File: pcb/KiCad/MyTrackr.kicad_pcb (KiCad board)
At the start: 2 copper layers, 50 x 50 mm, 38 parts, among them CN1 GPS_ANTENNA, CON1 MICRO_SD, J1 10A45B_Module, J2 CONN_ICSP, J3 CONN_01X05, J4 CONN_BAT, P1 CONN_OLED, Q1 Q_PMOS_GSD, SW1 BTN_RESET, SW2 BTN_SEL, SW3 BTN_NEXT, SW4 BTN_PREV, SW5 BTN_BACK, U1 ATMEGA48_88_168_328P-32SMD, U2 GPS-NEO-6M, U3 24AA32

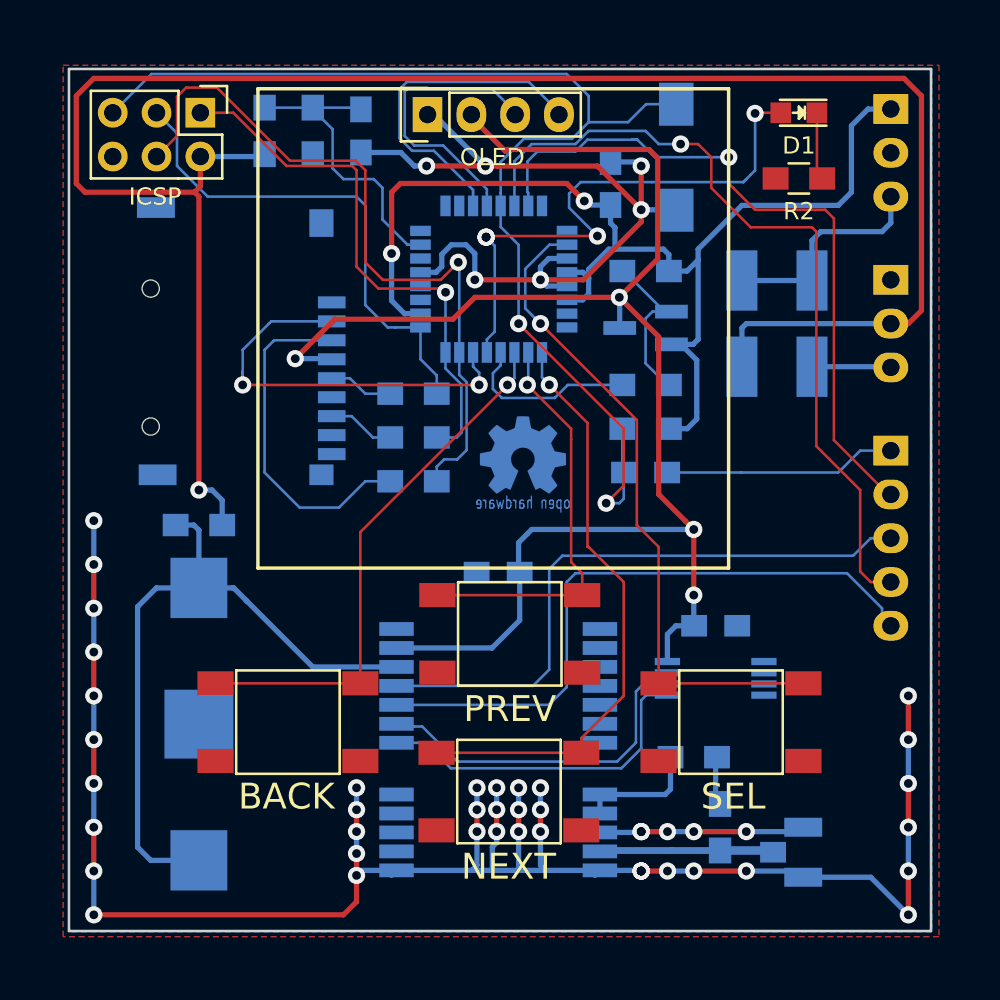
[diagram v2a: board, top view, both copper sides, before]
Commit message: Add screw holes, smooth corners and more
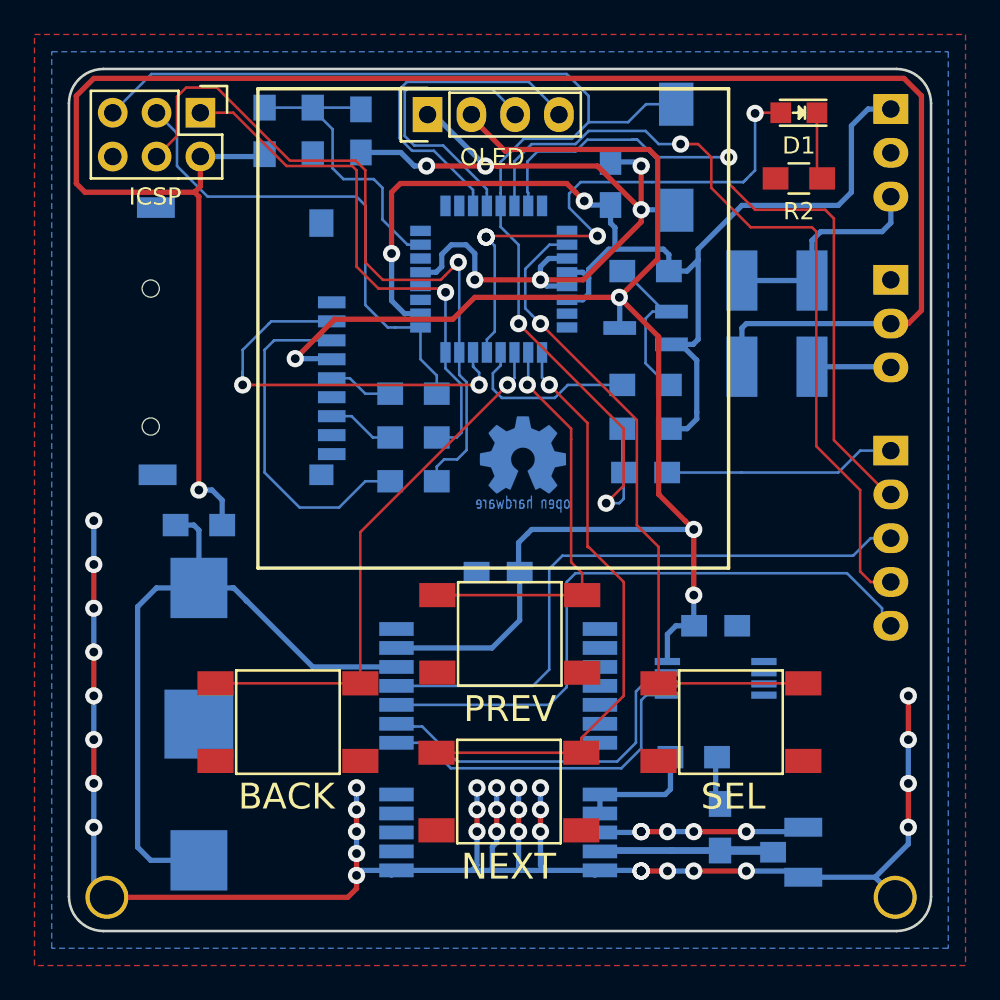
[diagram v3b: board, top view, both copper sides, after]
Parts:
- added P2: CONN_01X01, Sukko:Screw_Hole_Plated_2mm, F.Cu at (137.9, 98.0)
- added P3: CONN_01X01, Sukko:Screw_Hole_Plated_2mm, F.Cu at (92.2, 98.0)
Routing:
- net GND: track 174.0 -> 169.4 mm, vias 51 -> 47
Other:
- outline, holes or cut-outs redrawn
- board text added: "github.com/SukkoPera/MyTrackr"
- board text removed: "https://github.com/SukkoPera/MyTrackr"
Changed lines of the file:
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@@
 (kicad_pcb (version 4) (host pcbnew 4.0.7)
   (general
-    (links 103)
-    (no_connects 0)
+    (links 107)
+    (no_connects 28)
     (area 89.924999 49.924999 140.075001 100.075001)
     (thickness 1.6)
-    (drawings 39)
-    (tracks 586)
+    (drawings 43)
+    (tracks 582)
     (zones 0)
-    (modules 38)
+    (modules 40)
     (nets 37)
   )
@@
     (mod_text_size 1 1)
     (mod_text_width 0.15)
-    (pad_size 2 0.8)
-    (pad_drill 0)
+    (pad_size 2.5 2.5)
+    (pad_drill 2)
     (pad_to_mask_clearance 0)
     (aux_axis_origin 0 0)
@@
     (tags "resistor 0805")
     (attr smd)
-    (fp_text reference JP1 (at 3.81 0) (layer B.SilkS)
+    (fp_text reference JP1 (at -3.81 0) (layer B.SilkS)
       (effects (font (size 1 1) (thickness 0.15)) (justify mirror))
     )
@@
     (at 127.508 85.344 270)
     (descr TSSOP-8)
-    (fp_text reference U3 (at -2.286 -3.556 360) (layer B.SilkS)
+    (fp_text reference U3 (at 0 -4.826 360) (layer B.SilkS)
       (effects (font (size 1 1) (thickness 0.15)) (justify mirror))
     )
@@
     (pad 8 smd rect (at -0.97536 2.79908 270) (size 0.4191 1.47066) (layers B.Cu B.Mask)
       (net 33 VPP))
-    (model walter/smd_dil/tssop-8.wrl
-      (at (xyz 0 0 0))
-      (scale (xyz 1 1 1))
-      (rotate (xyz 0 0 0))
-    )
-  )
+    (model /home/sukko/Documents/kicad/lib/kicad_libs/modules/packages3d/walter/smd_dil/tssop-8.wrl
+      (at (xyz 0 0 0))
+      (scale (xyz 1 1 1))
+      (rotate (xyz 0 0 0))
+    )
+  )
+  (module Sukko:Screw_Hole_Plated_2mm (layer F.Cu)
+    (at 137.922 98.044)
+    (fp_text reference P2 (at 0 2.54) (layer F.SilkS) hide
+      (effects (font (size 1 1) (thickness 0.15)))
+    )
+    (fp_text value CONN_01X01 (at 0 5.08) (layer F.Fab) hide
+      (effects (font (size 1 1) (thickness 0.15)))
+    )
+    (pad 1 thru_hole circle (at 0 0) (size 2.5 2.5) (drill 2) (layers *.Cu *.Mask)
+      (net 2 GND) (zone_connect 2))
+  )
+  (module Sukko:Screw_Hole_Plated_2mm (layer F.Cu)
+    (at 92.202 98.044)
+    (fp_text reference P3 (at 0 2.54) (layer F.SilkS) hide
+      (effects (font (size 1 1) (thickness 0.15)))
+    )
+    (fp_text value CONN_01X01 (at 0 5.08) (layer F.Fab) hide
+      (effects (font (size 1 1) (thickness 0.15)))
+    )
+    (pad 1 thru_hole circle (at 0 0) (size 2.5 2.5) (drill 2) (layers *.Cu *.Mask)
+      (net 2 GND) (zone_connect 2))
+  )
+  (gr_arc (start 92 52) (end 90 52) (angle 90) (layer Edge.Cuts) (width 0.15))
+  (gr_arc (start 138 52) (end 138 50) (angle 90) (layer Edge.Cuts) (width 0.15))
+  (gr_arc (start 138 98) (end 140 98) (angle 90) (layer Edge.Cuts) (width 0.15))
+  (gr_arc (start 92 98) (end 92 100) (angle 90) (layer Edge.Cuts) (width 0.15))
   (gr_text OLED (at 114.554 55.118) (layer F.SilkS)
     (effects (font (size 1 1) (thickness 0.15)))
@@
     (effects (font (size 1 1) (thickness 0.15)))
   )
-  (gr_text Vi (at 135.474 57.404 360) (layer B.SilkS)
+  (gr_text Vi (at 135.474 57.404) (layer B.SilkS)
     (effects (font (size 0.7 0.7) (thickness 0.1)) (justify mirror))
   )
@@
     (effects (font (size 1 1) (thickness 0.15)) (justify mirror))
   )
-  (gr_text V1.1 (at 93.726 98.806) (layer B.SilkS)
+  (gr_text V1.1 (at 95.25 98.806) (layer B.SilkS)
     (effects (font (size 1 1) (thickness 0.15)) (justify mirror))
   )
@@
     (effects (font (size 0.7 0.7) (thickness 0.1)) (justify mirror))
   )
-  (gr_text https://github.com/SukkoPera/MyTrackr (at 115.316 98.806) (layer B.SilkS)
+  (gr_text github.com/SukkoPera/MyTrackr (at 115.316 98.806) (layer B.SilkS)
     (effects (font (size 1 1) (thickness 0.15)) (justify mirror))
   )
@@
   (gr_line (start 139.149 58.89) (end 139.149 51.27) (layer B.SilkS) (width 0.2))
   (gr_line (start 127.973 51.27) (end 127.973 58.89) (layer B.SilkS) (width 0.2))
-  (gr_line (start 140 100) (end 140 50) (layer Edge.Cuts) (width 0.15))
-  (gr_line (start 90 50) (end 90 100) (layer Edge.Cuts) (width 0.15))
-  (gr_line (start 140 50) (end 90 50) (layer Edge.Cuts) (width 0.15))
-  (gr_line (start 90 100) (end 140 100) (layer Edge.Cuts) (width 0.15))
+  (gr_line (start 140 98) (end 140 52) (layer Edge.Cuts) (width 0.15))
+  (gr_line (start 90 52) (end 90 98) (layer Edge.Cuts) (width 0.15))
+  (gr_line (start 138 50) (end 92 50) (layer Edge.Cuts) (width 0.15))
+  (gr_line (start 92 100) (end 138 100) (layer Edge.Cuts) (width 0.15))
   (gr_line (start 100.9592 51.1476) (end 100.9592 78.9476) (layer F.SilkS) (width 0.2))
   (gr_line (start 128.2592 51.1476) (end 100.9592 51.1476) (layer F.SilkS) (width 0.2))
@@
   (segment (start 129.286 64.77) (end 129.032 65.024) (width 0.3048) (layer B.Cu) (net 1))
   (segment (start 129.032 65.024) (end 129.032 67.26936) (width 0.3048) (layer B.Cu) (net 1))
+  (segment (start 106.68 96.774) (end 106.68 97.536) (width 0.3048) (layer F.Cu) (net 2))
+  (segment (start 106.172 98.044) (end 106.68 97.536) (width 0.3048) (layer F.Cu) (net 2))
+  (segment (start 92.202 98.044) (end 106.172 98.044) (width 0.3048) (layer F.Cu) (net 2))
+  (segment (start 91.44 93.98) (end 91.44 97.282) (width 0.3048) (layer B.Cu) (net 2))
+  (segment (start 91.44 97.282) (end 92.202 98.044) (width 0.3048) (layer B.Cu) (net 2))
+  (segment (start 138.684 93.98) (end 138.684 94.954) (width 0.3048) (layer B.Cu) (net 2))
+  (segment (start 138.684 94.954) (end 136.758 96.88) (width 0.3048) (layer B.Cu) (net 2))
+  (segment (start 132.588 96.88) (end 136.758 96.88) (width 0.3048) (layer B.Cu) (net 2))
+  (segment (start 136.758 96.88) (end 138.176 98.298) (width 0.3048) (layer B.Cu) (net 2))
   (segment (start 123.19 55.626) (end 123.19 58.166) (width 0.3048) (layer F.Cu) (net 2))
   (segment (start 121.412 55.392) (end 122.956 55.392) (width 0.3048) (layer B.Cu) (net 2))
@@
   (segment (start 138.684 93.98) (end 138.684 91.44) (width 0.3048) (layer F.Cu) (net 2))
   (via (at 138.684 91.44) (size 1) (drill 0.508) (layers F.Cu B.Cu) (net 2))
-  (segment (start 138.684 96.52) (end 138.684 93.98) (width 0.3048) (layer B.Cu) (net 2))
   (via (at 138.684 93.98) (size 1) (drill 0.508) (layers F.Cu B.Cu) (net 2))
-  (segment (start 138.684 99.06) (end 138.684 96.52) (width 0.3048) (layer F.Cu) (net 2))
-  (via (at 138.684 96.52) (size 1) (drill 0.508) (layers F.Cu B.Cu) (net 2))
-  (segment (start 132.588 96.88) (end 136.504 96.88) (width 0.3048) (layer B.Cu) (net 2))
-  (segment (start 136.504 96.88) (end 138.684 99.06) (width 0.3048) (layer B.Cu) (net 2))
-  (via (at 138.684 99.06) (size 1) (drill 0.508) (layers F.Cu B.Cu) (net 2))
   (segment (start 91.44 78.74) (end 91.44 76.2) (width 0.3048) (layer B.Cu) (net 2))
   (via (at 91.44 76.2) (size 1) (drill 0.508) (layers F.Cu B.Cu) (net 2))
@@
   (segment (start 91.44 93.98) (end 91.44 91.44) (width 0.3048) (layer B.Cu) (net 2))
   (via (at 91.44 91.44) (size 1) (drill 0.508) (layers F.Cu B.Cu) (net 2))
-  (segment (start 91.44 96.52) (end 91.44 93.98) (width 0.3048) (layer F.Cu) (net 2))
   (via (at 91.44 93.98) (size 1) (drill 0.508) (layers F.Cu B.Cu) (net 2))
-  (segment (start 91.44 99.06) (end 91.44 96.52) (width 0.3048) (layer B.Cu) (net 2))
-  (via (at 91.44 96.52) (size 1) (drill 0.508) (layers F.Cu B.Cu) (net 2))
-  (segment (start 105.918 99.06) (end 91.44 99.06) (width 0.3048) (layer F.Cu) (net 2))
-  (via (at 91.44 99.06) (size 1) (drill 0.508) (layers F.Cu B.Cu) (net 2))
-  (segment (start 106.68 98.298) (end 105.918 99.06) (width 0.3048) (layer F.Cu) (net 2))
-  (segment (start 106.68 96.774) (end 106.68 98.298) (width 0.3048) (layer F.Cu) (net 2))
   (segment (start 113.665 92.964) (end 113.665 91.694) (width 0.3048) (layer B.Cu) (net 2))
   (via (at 113.665 91.694) (size 1) (drill 0.508) (layers F.Cu B.Cu) (net 2))
@@
     (polygon
       (pts
-        (xy 140.462 100.33) (xy 89.662 100.33) (xy 89.662 49.784) (xy 140.462 49.784)
+        (xy 142 102) (xy 88 102) (xy 88 48) (xy 142 48)
       )
     )
@@
     (polygon
       (pts
-        (xy 140.038 100.038) (xy 90 100.038) (xy 90 50) (xy 140.038 50)
+        (xy 141 101) (xy 89 101) (xy 89 49) (xy 141 49)
       )
     )

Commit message: Move project to KiCad 5.1.9, make all libs/footprints local
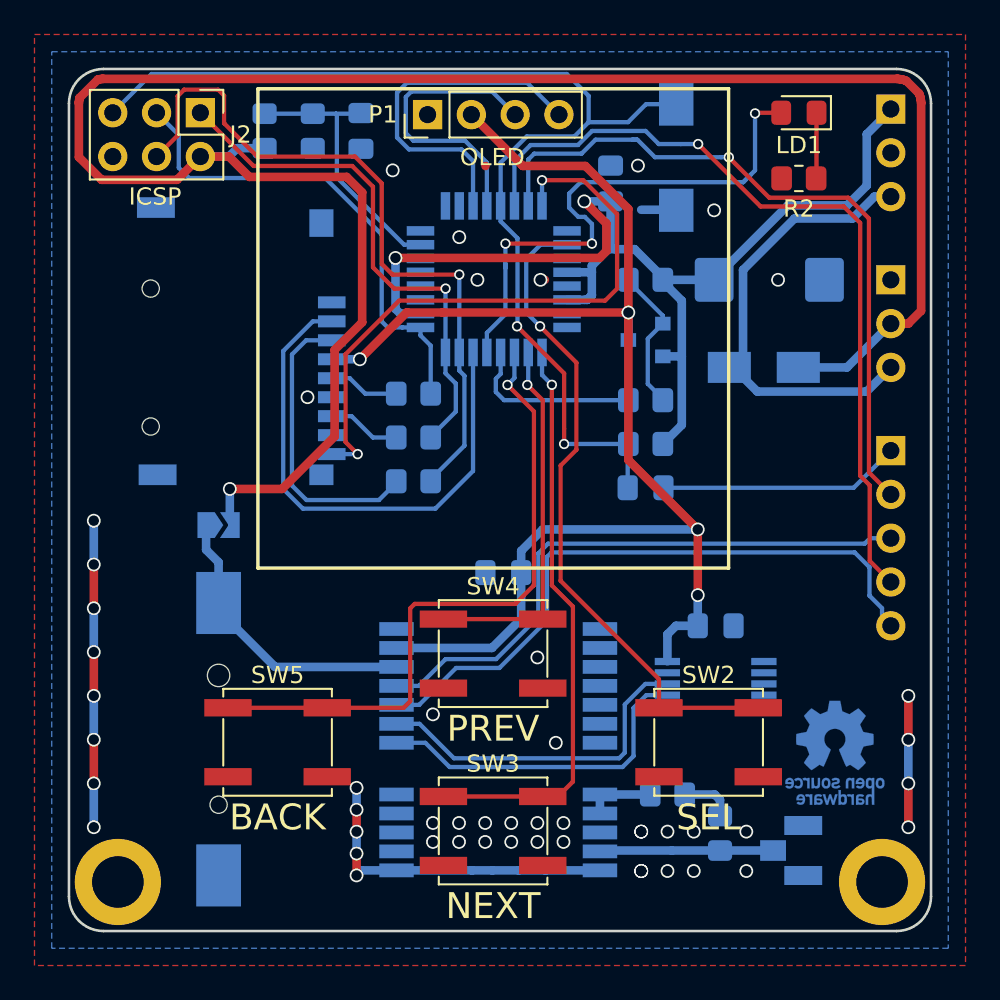
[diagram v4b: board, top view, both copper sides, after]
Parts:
- removed BT2: GPS_BKP, Battery_Holders:Keystone_3000_1x12mm-CoinCell
- removed D2, D3: D_Schottky, Diodes_SMD:SMA_Handsoldering
- removed G***: LOGO, w_logo:Logo_copper_OSHW_6x6mm
- removed P2, P3: CONN_01X01, Sukko:Screw_Hole_Plated_2mm
- added BT1: GPS_BKP, MyTrackr:BR1225A_KEYSTONE_1056, B.Cu at (98.7, 88.9)
- added C6: CP1_Small, Capacitor_Tantalum_SMD:CP_EIA-7343-30_AVX-N_Pad2.25x2.55mm_HandSolder, B.Cu at (130.6, 62.2)
- added H1: MountingHole_Pad, MyTrackr:Screw_Hole_Plated_3mm, F.Cu at (92.8, 97.2)
- added H2: MountingHole_Pad, MyTrackr:Screw_Hole_Plated_3mm, F.Cu at (137.2, 97.2)
- added LD1: LED, LED_SMD:LED_0805_2012Metric_Pad1.15x1.40mm_HandSolder, F.Cu at (132.3, 52.5)
- added V0: OSHW_LOGO, Symbol:OSHW-Logo_5.7x6mm_Copper, B.Cu at (134.4, 89.7)
- C1, C2, C3, C4, C5: footprint Capacitors_SMD:C_0805_HandSoldering -> Capacitor_SMD:C_0805_2012Metric_Pad1.18x1.45mm_HandSolder
- CN1: footprint MyKiCadLibs-Footprints:CONN-RF-UFL -> MyTrackr:CONN-RF-UFL
- CON1: footprint MicroSD GCT-MEM2055-00-190-01-A:GCT-MEM2055-00-190-01-A -> MyTrackr:GCT-MEM2055-00-190-01-A
- D1: value LED -> SS24; footprint LEDs:LED_0805 -> Diode_SMD:D_SMA; moved to B.Cu
- J1: value 10A45B_Module -> REGULATOR_3V3; footprint Pin_Headers:Pin_Header_Straight_1x03 -> Connector_PinHeader_2.54mm:PinHeader_1x03_P2.54mm_Vertical
- J2: footprint Pin_Headers:Pin_Header_Straight_2x03 -> Connector_PinHeader_2.54mm:PinHeader_2x03_P2.54mm_Vertical
- J3: value CONN_01X05 -> CONN_SERIAL; footprint Pin_Headers:Pin_Header_Straight_1x05 -> Connector_PinHeader_2.54mm:PinHeader_1x05_P2.54mm_Vertical
- J4: footprint Pin_Headers:Pin_Header_Straight_1x03 -> Connector_PinHeader_2.54mm:PinHeader_1x03_P2.54mm_Vertical
- JP1: value NO -> JMP_BAT; footprint Resistors_SMD:R_0805_HandSoldering -> Jumper:SolderJumper-2_P1.3mm_Open_TrianglePad1.0x1.5mm
- L1: value 22u -> 22; footprint Resistors_SMD:R_0805_HandSoldering -> Resistor_SMD:R_0805_2012Metric_Pad1.20x1.40mm_HandSolder
- P1: footprint Pin_Headers:Pin_Header_Straight_1x04 -> Connector_PinHeader_2.54mm:PinHeader_1x04_P2.54mm_Vertical
- Q1: footprint TO_SOT_Packages_SMD:SOT-23_Handsoldering -> Package_TO_SOT_SMD:SOT-23
- R1, R10, R2, R3, R4, R5, R6, R7, R8, R9: footprint Resistors_SMD:R_0805_HandSoldering -> Resistor_SMD:R_0805_2012Metric_Pad1.20x1.40mm_HandSolder
- SW1: footprint Buttons_Switches_SMD:SW_SPST_REED_CT05-XXXX-J1 -> Button_Switch_SMD:SW_SPST_REED_CT05-XXXX-J1
- SW2, SW3, SW4, SW5: footprint MyKiCadLibs-Footprints:SW_TACT_SMD -> Button_Switch_SMD:SW_SPST_EVPBF
- U1: footprint Housings_QFP:LQFP-32_7x7mm_Pitch0.8mm -> Package_QFP:TQFP-32_7x7mm_P0.8mm
- U2: footprint MOUDLE-GPS-NEO-6M_24P-16X12.2MM_:GPS24P-SMD-1.1-16X12.2MM -> MyTrackr:GPS24P-SMD-1.1-16X12.2MM
- moved D1 14.9 mm to (130.3, 67.3), turned to 0 degrees
- moved R3 2.65 mm to (124.7, 92.1)
- moved SW3 2.46 mm to (114.6, 94.2), turned to 0 degrees
- moved SW2 1.75 mm to (127.1, 89.1), turned to 0 degrees
- moved SW4 1.50 mm to (114.6, 83.9), turned to 0 degrees
- moved SW5 1.31 mm to (102.1, 89.1), turned to 0 degrees
- moved JP1 1.14 mm to (98.7, 76.5)
- moved C1 0.88 mm to (123.4, 74.3)
- moved R1 0.88 mm to (123.4, 71.8), turned to 180 degrees
- moved R10 0.88 mm to (123.4, 69.2), turned to 180 degrees
- moved Q1 0.70 mm to (123.4, 65.7)
- moved R9 0.51 mm to (123.4, 62.2), turned to 180 degrees
- moved L1 0.35 mm to (127.8, 94.3)
- moved C3 0.30 mm to (115.2, 79.2)
- moved CN1 0.10 mm to (132.6, 97.3)
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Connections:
- C4 pad 1: GND -> VPP
- C4 pad 2: VPP -> GND
- CON1 pad 10: (no net) -> GND
- CON1 pad 9: GND -> /CARD_DETECT
- D1 pad 1: Net-(D1-Pad1) -> /VCHG
- D1 pad 2: /ARDUINO_PIN_9 -> /VBAT
- J1 pad 3: Net-(D2-Pad1) -> /VCHG
- R1 pad 1: /RESET -> +3V3
- R1 pad 2: +3V3 -> /RESET
- R10 pad 1: /ARDUINO_PIN_8 -> Net-(Q1-Pad1)
- R10 pad 2: Net-(Q1-Pad1) -> /ARDUINO_PIN_8
- R2 pad 1: Net-(D1-Pad1) -> GND
- R2 pad 2: GND -> Net-(LD1-Pad1)
- R4 pad 1: Net-(C5-Pad1) -> /VBAT
- R4 pad 2: /VBAT -> Net-(C5-Pad1)
- R5 pad 1: GND -> Net-(C5-Pad1)
- R5 pad 2: Net-(C5-Pad1) -> GND
- R6 pad 1: /MOSI -> /DATA_IN
- R6 pad 2: /DATA_IN -> /MOSI
- R7 pad 1: /SCK -> /CLK
- R7 pad 2: /CLK -> /SCK
- R8 pad 1: /MISO -> /DATA_OUT
- R8 pad 2: /DATA_OUT -> /MISO
- R9 pad 1: Net-(Q1-Pad1) -> +3V3
- R9 pad 2: +3V3 -> Net-(Q1-Pad1)
- U1 pad 32: (no net) -> /CARD_DETECT
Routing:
- net GND: track 169.4 -> 51.2 mm, vias 47 -> 51
- net /CARD_DETECT: track 0.00 -> 35.9 mm, vias 0 -> 2
- net Net-(BT1-Pad1): track 39.9 -> 16.5 mm
- net /VCHG: track 5.10 -> 27.3 mm
- net Net-(D2-Pad1): track 12.9 -> 0.00 mm
- net VPP: track 92.2 -> 83.5 mm
- net /CS: track 23.9 -> 30.8 mm, vias 2 -> 0
- net /ARDUINO_PIN_7: track 31.3 -> 38.2 mm
- net /VBAT: track 113.9 -> 120.0 mm
- net /RESET: track 70.6 -> 66.2 mm
- net Net-(LD1-Pad1): track 0.00 -> 4.25 mm
- net Net-(D1-Pad1): track 3.93 -> 0.00 mm
- net Net-(R3-Pad2): track 7.18 -> 4.02 mm
- net /DATA_IN: track 20.1 -> 17.2 mm
- net +3V3: track 67.8 -> 65.6 mm
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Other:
- net class Antenna: clearance 0.15 -> 0.25; trace_width 0.4 -> 0.5; via_dia 1 -> 0.8; via_drill 0.508 -> 0.6
- net class Default: clearance 0.1524 -> 0.25; trace_width 0.1524 -> 0.25; via_dia 1 -> 0.6; via_drill 0.508 -> 0.4
- net class Power: clearance 0.1524 -> 0.25; trace_width 0.3048 -> 0.5; via_dia 1 -> 0.8; via_drill 0.508 -> 0.6
- rule trace_clearance: 0.1524 -> 0.25
- board text added: "V2"
- board text removed: "BAT"
- board text removed: "V1.1"

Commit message: Remove old cruft
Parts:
- U1: value ATMEGA48_88_168_328P-32SMD -> ATMEGA328PA
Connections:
- U1 pad 21: GND -> (no net)
- U1 pad 5: GND -> (no net)
